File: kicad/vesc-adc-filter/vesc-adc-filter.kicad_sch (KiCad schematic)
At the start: 7 parts, among them J3 PWM

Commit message: Added encoder breakout and updated other projects
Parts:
- H1, H2: footprint MountingHole:MountingHole_3.2mm_M3 -> MountingHole:MountingHole_3.2mm_M3_Pad_Via
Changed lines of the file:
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@@
       (effects (font (size 1.27 1.27)) (justify left))
     )
-    (property "Footprint" "MountingHole:MountingHole_3.2mm_M3" (at 152.4 107.95 0)
+    (property "Footprint" "MountingHole:MountingHole_3.2mm_M3_Pad_Via" (at 152.4 107.95 0)
       (effects (font (size 1.27 1.27)) hide)
     )
@@
       (effects (font (size 1.27 1.27)) (justify left))
     )
-    (property "Footprint" "MountingHole:MountingHole_3.2mm_M3" (at 152.4 100.33 0)
+    (property "Footprint" "MountingHole:MountingHole_3.2mm_M3_Pad_Via" (at 152.4 100.33 0)
       (effects (font (size 1.27 1.27)) hide)
     )

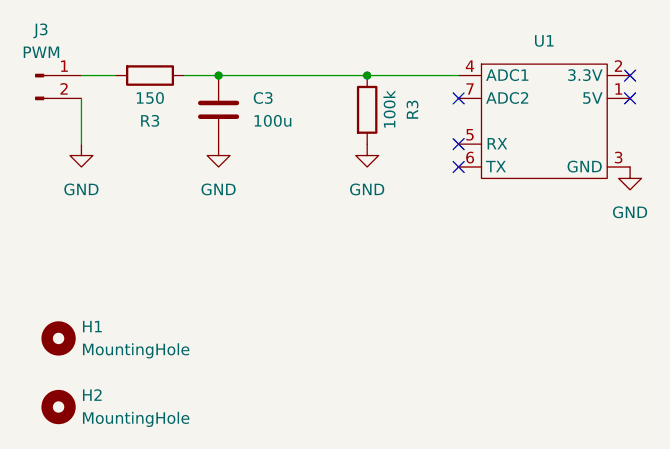
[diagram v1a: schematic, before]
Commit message: Changes after manufacting
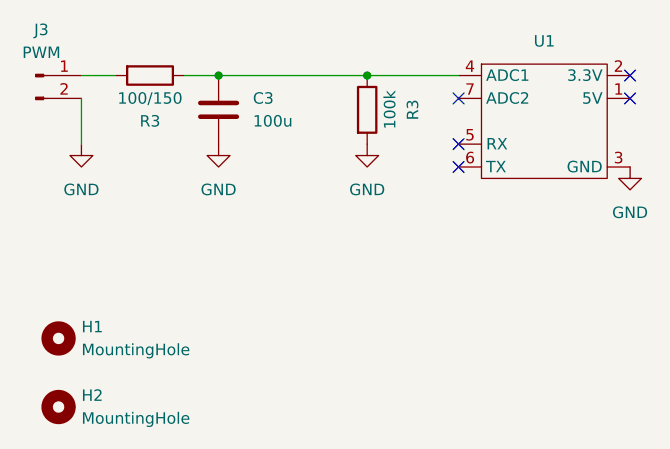
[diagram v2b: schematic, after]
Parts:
- R3: value 150 -> 100/150
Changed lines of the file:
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@@
       (effects (font (size 1.27 1.27)))
     )
-    (property "Value" "150" (at 162.56 73.66 90)
+    (property "Value" "100/150" (at 162.56 73.66 90)
       (effects (font (size 1.27 1.27)))
     )
